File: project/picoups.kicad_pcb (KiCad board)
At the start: 4 copper layers, 65 x 30 mm, 73 parts, among them J1 VIN, J2 BATT, J3 USB_C_Receptacle, J4 Conn_02x20_Odd_Even, Q1 Q_PMOS_GSD, SW1 SW_5V, SW2 SW_USER, U1 LT3652EMSE, U2 TPS2116, U3 TPS61235P, U4 BQ24040, U5 INA3221, U6 M41T62

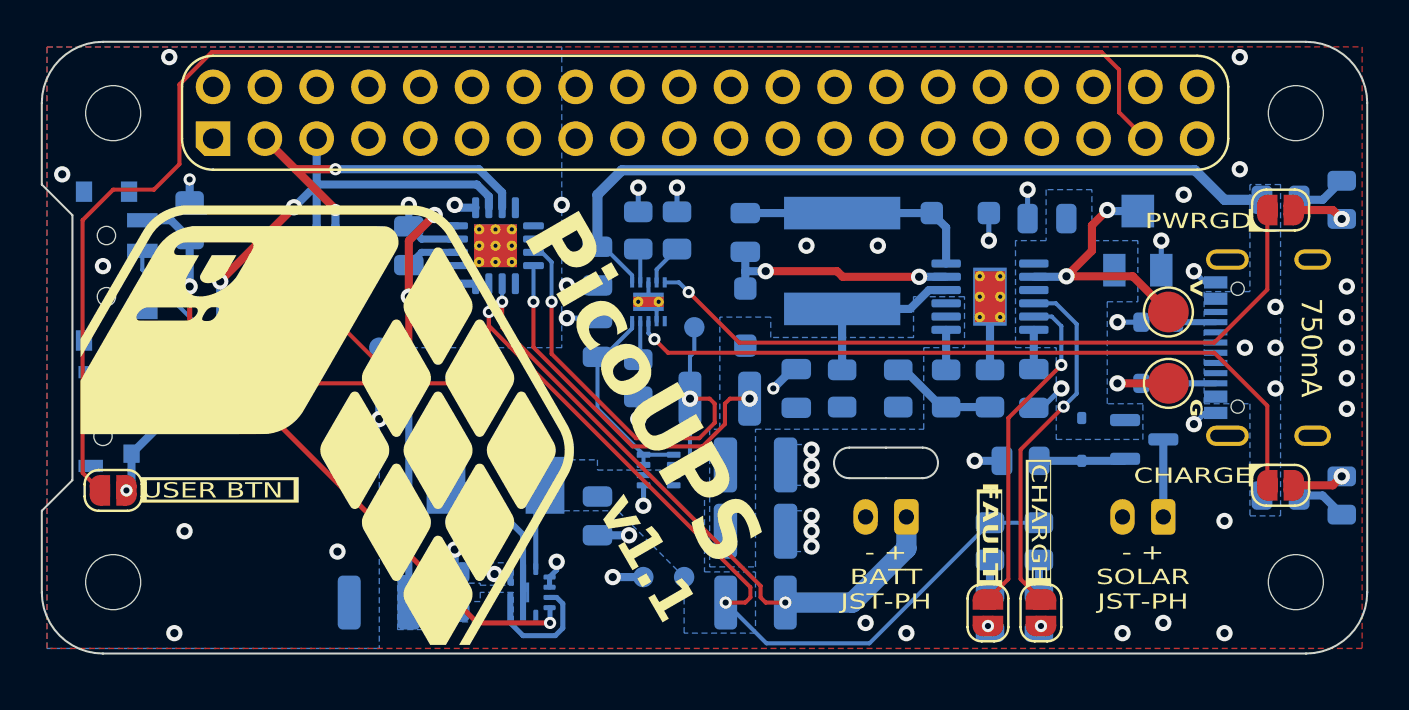
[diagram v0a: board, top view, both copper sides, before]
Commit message: Fixed solar status LEDs wrong VBAT
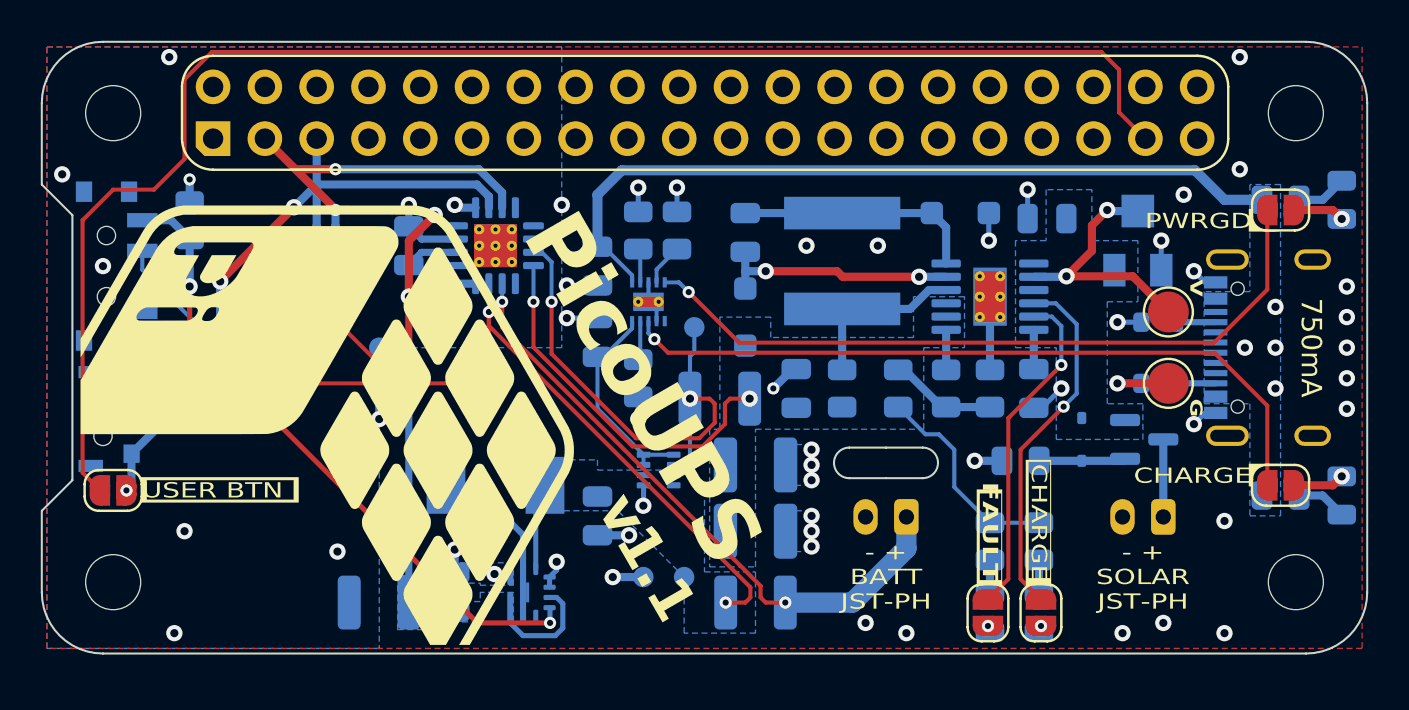
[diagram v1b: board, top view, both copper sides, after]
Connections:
- J4 pad 1: 3v3 -> unconnected-(J4-Pin_1-Pad1)
- R16 pad 2: VBAT+ -> VBAT_SOL+
- R17 pad 2: VBAT+ -> VBAT_SOL+
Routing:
- net VBAT+: track 74.3 -> 55.6 mm
- net VBAT_SOL+: track 18.2 -> 28.5 mm
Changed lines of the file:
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@@
   (net 29 "unconnected-(J3-SBU2-PadB8)")
   (net 30 "unconnected-(J3-SHIELD-PadS1)")
-  (net 31 "3v3")
+  (net 31 "unconnected-(J4-Pin_1-Pad1)")
   (net 32 "5V")
   (net 33 "SDA")
@@
     (pad "1" thru_hole roundrect (at -2.54 0 90) (size 1.7 1.7) (drill 1) (layers "*.Cu" "*.Mask") (roundrect_rratio 0)
       (chamfer_ratio 0.25) (chamfer top_left)
-      (net 31 "3v3") (pinfunction "Pin_1") (pintype "passive"))
+      (net 31 "unconnected-(J4-Pin_1-Pad1)") (pinfunction "Pin_1") (pintype "passive+no_connect"))
     (pad "2" thru_hole circle (at 0 0 90) (size 1.7 1.7) (drill 1) (layers "*.Cu" "*.Mask")
       (net 32 "5V") (pinfunction "Pin_2") (pintype "passive"))
@@
     (pad "17" thru_hole circle (at 0.8 0.8) (size 0.5 0.5) (drill 0.2) (layers "*.Cu")
       (net 1 "GND") (pinfunction "EP") (pintype "passive"))
-    (model "${KICAD7_3DMODEL_DIR}/Package_DFN_QFN.3dshapes/QFN-16-1EP_4x4mm_P0.65mm_EP2.1x2.1mm.step"
+    (model "${KICAD6_3DMODEL_DIR}/Package_DFN_QFN.3dshapes/Texas_RGV_S-PVQFN-N16_EP2.1x2.1mm.wrl"
       (offset (xyz 0 0 0))
       (scale (xyz 1 1 1))
@@
       (net 15 "Net-(D5-A)") (pintype "passive"))
     (pad "2" smd roundrect (at 0.9125 0 90) (size 1.025 1.4) (layers "B.Cu" "B.Paste" "B.Mask") (roundrect_rratio 0.243902439)
-      (net 7 "VBAT+") (pintype "passive"))
+      (net 3 "VBAT_SOL+") (pintype "passive"))
     (model "${KICAD6_3DMODEL_DIR}/Resistor_SMD.3dshapes/R_0805_2012Metric.wrl"
       (offset (xyz 0 0 0))
@@
       (net 13 "Net-(D4-A)") (pintype "passive"))
     (pad "2" smd roundrect (at 0.9125 0 90) (size 1.025 1.4) (layers "B.Cu" "B.Paste" "B.Mask") (roundrect_rratio 0.243902439)
-      (net 7 "VBAT+") (pintype "passive"))
+      (net 3 "VBAT_SOL+") (pintype "passive"))
     (model "${KICAD6_3DMODEL_DIR}/Resistor_SMD.3dshapes/R_0805_2012Metric.wrl"
       (offset (xyz 0 0 0))
@@
   (via (at 115.1125 104.75) (size 0.6) (drill 0.3) (layers "F.Cu" "B.Cu") (net 3))
   (via (at 125.7125 109.5) (size 0.8) (drill 0.4) (layers "F.Cu" "B.Cu") (net 3))
+  (segment (start 137.5 115.5875) (end 135.75 113.8375) (width 0.2) (layer "B.Cu") (net 3))
+  (segment (start 134.3375 111.25) (end 133 109.9125) (width 0.2) (layer "B.Cu") (net 3))
+  (segment (start 135.75 113.8375) (end 135.75 112) (width 0.2) (layer "B.Cu") (net 3))
+  (segment (start 139.9 115.5875) (end 137.5 115.5875) (width 0.2) (layer "B.Cu") (net 3))
+  (segment (start 135.75 112) (end 135 111.25) (width 0.2) (layer "B.Cu") (net 3))
   (segment (start 115.1125 104.75) (end 115.1125 102.975) (width 0.2) (layer "B.Cu") (net 3))
+  (segment (start 135 111.25) (end 134.3375 111.25) (width 0.2) (layer "B.Cu") (net 3))
   (segment (start 134.644916 100.4) (end 130.25 100.4) (width 0.4) (layer "B.Cu") (net 4))
   (segment (start 135.35 102.875) (end 135.35 101.105084) (width 0.4) (layer "B.Cu") (net 4))
@@
   (via (at 124.5375 119.5) (size 0.6) (drill 0.3) (layers "F.Cu" "B.Cu") (net 7))
   (via (at 99 106.25) (size 0.6) (drill 0.3) (layers "F.Cu" "B.Cu") (net 7))
-  (segment (start 131.5875 121.5) (end 126.5375 121.5) (width 0.2) (layer "B.Cu") (net 7))
   (segment (start 112.925 105.25) (end 112.925 103.8625) (width 0.2) (layer "B.Cu") (net 7))
   (segment (start 115.225 117.85) (end 115.225 114.2015) (width 0.25) (layer "B.Cu") (net 7))
-  (segment (start 137.5 115.5875) (end 131.5875 121.5) (width 0.2) (layer "B.Cu") (net 7))
   (segment (start 104.48 104.73) (end 104.48 103.85) (width 0.2) (layer "B.Cu") (net 7))
   (segment (start 115.225 114.2015) (end 115.6765 113.75) (width 0.25) (layer "B.Cu") (net 7))
-  (segment (start 139.9 115.5875) (end 137.5 115.5875) (width 0.2) (layer "B.Cu") (net 7))
   (segment (start 95.93 103.18) (end 95.93 102.25) (width 0.2) (layer "B.Cu") (net 7))
-  (segment (start 126.5375 121.5) (end 124.5375 119.5) (width 0.2) (layer "B.Cu") (net 7))
   (segment (start 99 106.25) (end 95.93 103.18) (width 0.2) (layer "B.Cu") (net 7))
   (segment (start 109 104.5) (end 109 107.75) (width 0.35) (layer "F.Cu") (net 8))
@@
   (segment (start 95.15 114) (end 95.4 113.75) (width 0.4) (layer "B.Cu") (net 34))
   (segment (start 99.75 103.75) (end 99.75 107.85) (width 0.4) (layer "B.Cu") (net 34))
-  (segment (start 143.83 93.366117) (end 143.83 95.46) (width 0.2) (layer "F.Cu") (net 59))
-  (segment (start 93.85 113.984314) (end 93 113.134314) (width 0.2) (layer "F.Cu") (net 59))
-  (segment (start 97.75 94.092233) (end 99.342233 92.5) (width 0.2) (layer "F.Cu") (net 59))
-  (segment (start 97.75 98) (end 97.75 94.092233) (width 0.2) (layer "F.Cu") (net 59))
   (segment (start 93 113.134314) (end 93 100.75) (width 0.2) (layer "F.Cu") (net 59))
-  (segment (start 99.342233 92.5) (end 142.963883 92.5) (width 0.2) (layer "F.Cu") (net 59))
-  (segment (start 94.5 99.25) (end 96.5 99.25) (width 0.2) (layer "F.Cu") (net 59))
-  (segment (start 96.5 99.25) (end 97.75 98) (width 0.2) (layer "F.Cu") (net 59))
-  (segment (start 143.83 95.46) (end 145.12 96.75) (width 0.2) (layer "F.Cu") (net 59))
   (segment (start 93 100.75) (end 94.5 99.25) (width 0.2) (layer "F.Cu") (net 59))
   (segment (start 142.963883 92.5) (end 143.83 93.366117) (width 0.2) (layer "F.Cu") (net 59))
+  (segment (start 98 93.842233) (end 99.342233 92.5) (width 0.2) (layer "F.Cu") (net 59))
+  (segment (start 98 97.75) (end 98 93.842233) (width 0.2) (layer "F.Cu") (net 59))
+  (segment (start 143.83 93.366117) (end 143.83 95.46) (width 0.2) (layer "F.Cu") (net 59))
+  (segment (start 94.5 99.25) (end 96.5 99.25) (width 0.2) (layer "F.Cu") (net 59))
+  (segment (start 143.83 95.46) (end 145.12 96.75) (width 0.2) (layer "F.Cu") (net 59))
+  (segment (start 96.5 99.25) (end 98 97.75) (width 0.2) (layer "F.Cu") (net 59))
+  (segment (start 99.342233 92.5) (end 142.963883 92.5) (width 0.2) (layer "F.Cu") (net 59))
+  (segment (start 93.85 113.984314) (end 93 113.134314) (width 0.2) (layer "F.Cu") (net 59))
   (segment (start 141 107.8495) (end 138.4 110.4495) (width 0.2) (layer "F.Cu") (net 62))
   (segment (start 138.4 118.35) (end 137.4 119.35) (width 0.2) (layer "F.Cu") (net 62))

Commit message: Moved 5V supply
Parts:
- added TP7: GND, TestPoint:TestPoint_Pad_D1.0mm, B.Cu at (116.2, 109.8)
- added TP9: 5V, TestPoint:TestPoint_Pad_D1.0mm, B.Cu at (116.2, 107.8)
- moved TP6 13.4 mm to (114.2, 107.8)
- moved TP5 10.6 mm to (114.2, 109.8)
- moved C7 5.76 mm to (121.5, 120.0), turned to 180 degrees
- moved TP3 4.71 mm to (112.2, 107.8)
- moved TP4 4.71 mm to (112.2, 109.8)
- moved C8 2.50 mm to (113.8, 119.0)
- moved L2 2.50 mm to (115.8, 113.8)
- moved U3 2.50 mm to (117.2, 119.0)
- moved R11 2.46 mm to (110.0, 119.5)
- moved U6 0.75 mm to (104.9, 101.8)
- moved R8 0.25 mm to (120.5, 108.5)
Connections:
- net /Power Mux/USB renamed VBAT_USB
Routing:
- net Net-(SW1-C): track 31.7 -> 40.0 mm
- net VBAT+: track 55.6 -> 50.3 mm
- net VBAT_USB: track 10.3 -> 12.5 mm
- net GND: track 45.6 -> 44.5 mm, vias 61 -> 35
- net SDA: track 17.3 -> 16.2 mm
- net 5V+: track 30.8 -> 31.9 mm, vias 3 -> 4
- net SCL: track 32.5 -> 31.8 mm
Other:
- board text added: "5"
- board text added: "B"
- board text added: "U"
- board text removed: "5V"
- board text removed: "GND"
- board text removed: "VBAT"

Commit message: Dimmed the USB status LEDs (again)
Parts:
- R18, R19: value 500 -> 1k
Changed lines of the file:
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@@
         (effects (font (size 0.6 0.8) (thickness 0.15)) (justify mirror))
     )
-    (fp_text value "500" (at 0 -1.65) (layer "B.Fab")
+    (fp_text value "1k" (at 0 -1.65) (layer "B.Fab")
         (effects (font (size 1 1) (thickness 0.15)) (justify mirror))
     )
@@
         (effects (font (size 0.6 0.8) (thickness 0.15) bold) (justify mirror))
     )
-    (fp_text value "500" (at 0 -1.65) (layer "B.Fab")
-        (effects (font (size 1 1) (thickness 0.15)) (justify mirror))
-    )
+    (fp_text value "1k" (at 0 -1.65) (layer "B.Fab")
+        (effects (font (size 1 1) (thickness 0.15)) (justify mirror))
+    )

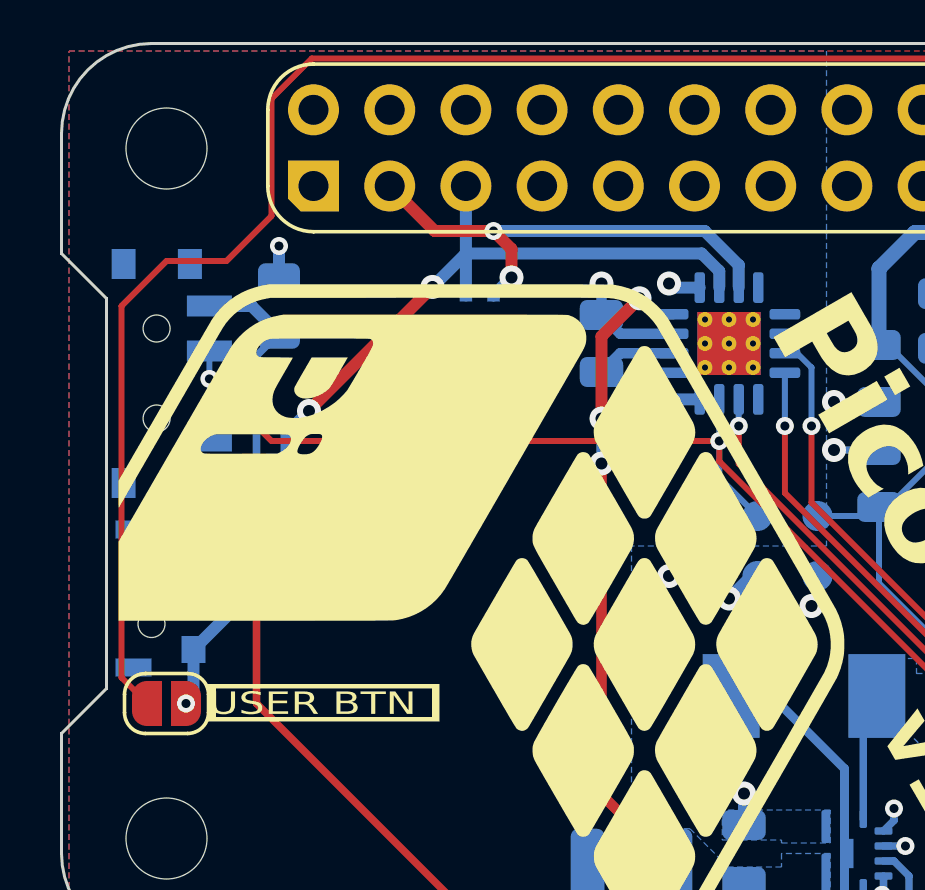
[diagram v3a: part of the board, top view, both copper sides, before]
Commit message: Added RTC wake
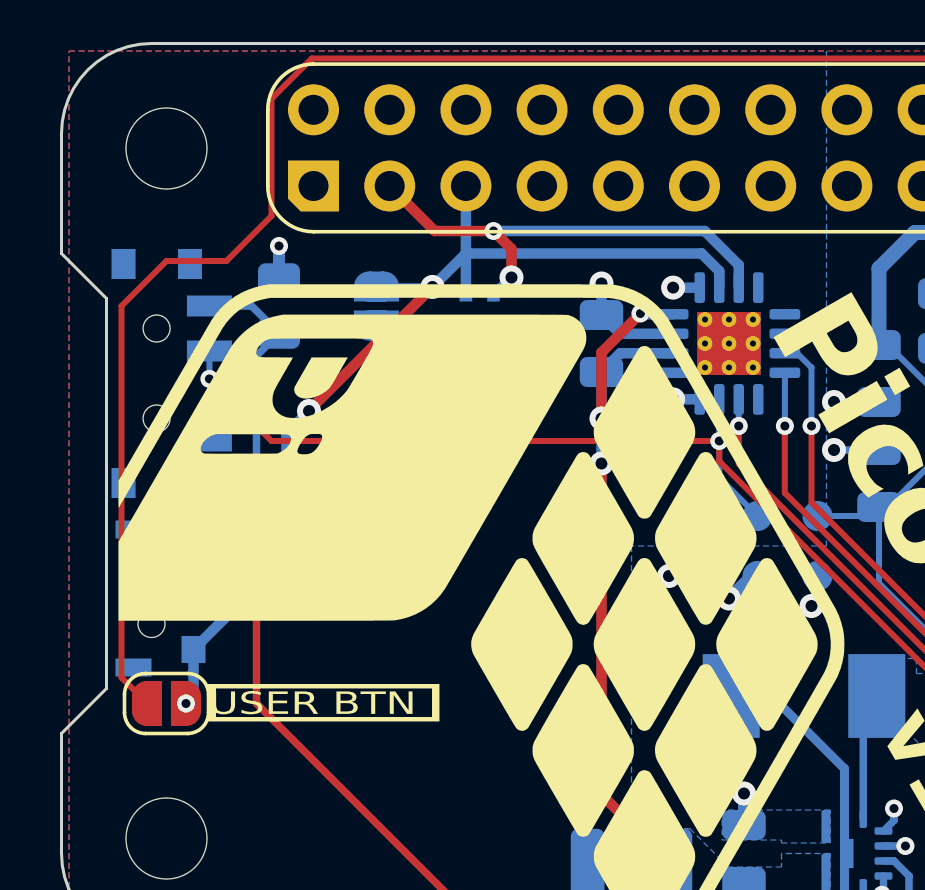
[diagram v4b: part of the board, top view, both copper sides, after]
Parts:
- added JP6: USER, Jumper:SolderJumper-2_P1.3mm_Open_RoundedPad1.0x1.5mm, B.Cu at (101.5, 100.8)
- moved G*** 1.00 mm to (100.8, 109.2)
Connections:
- U6 pad 6: unconnected-(U6-~{IRQ}/OUT-Pad6) -> WAKEUP
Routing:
- net WAKEUP: track 0.00 -> 3.31 mm
- net SCL: track 31.8 -> 33.6 mm
- net 5V+: track 31.9 -> 31.1 mm
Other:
- board text added: "RTC WAKE"

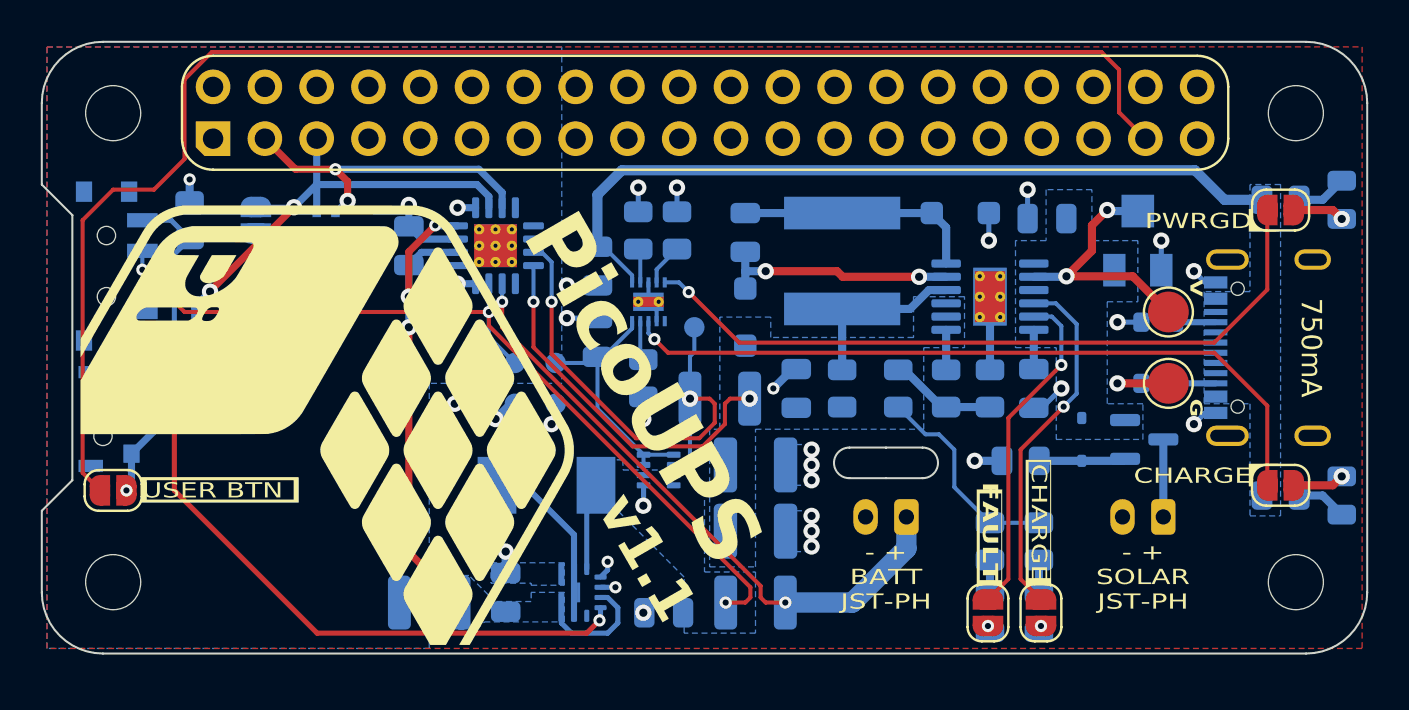
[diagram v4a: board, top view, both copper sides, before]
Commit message: Added output capacitors
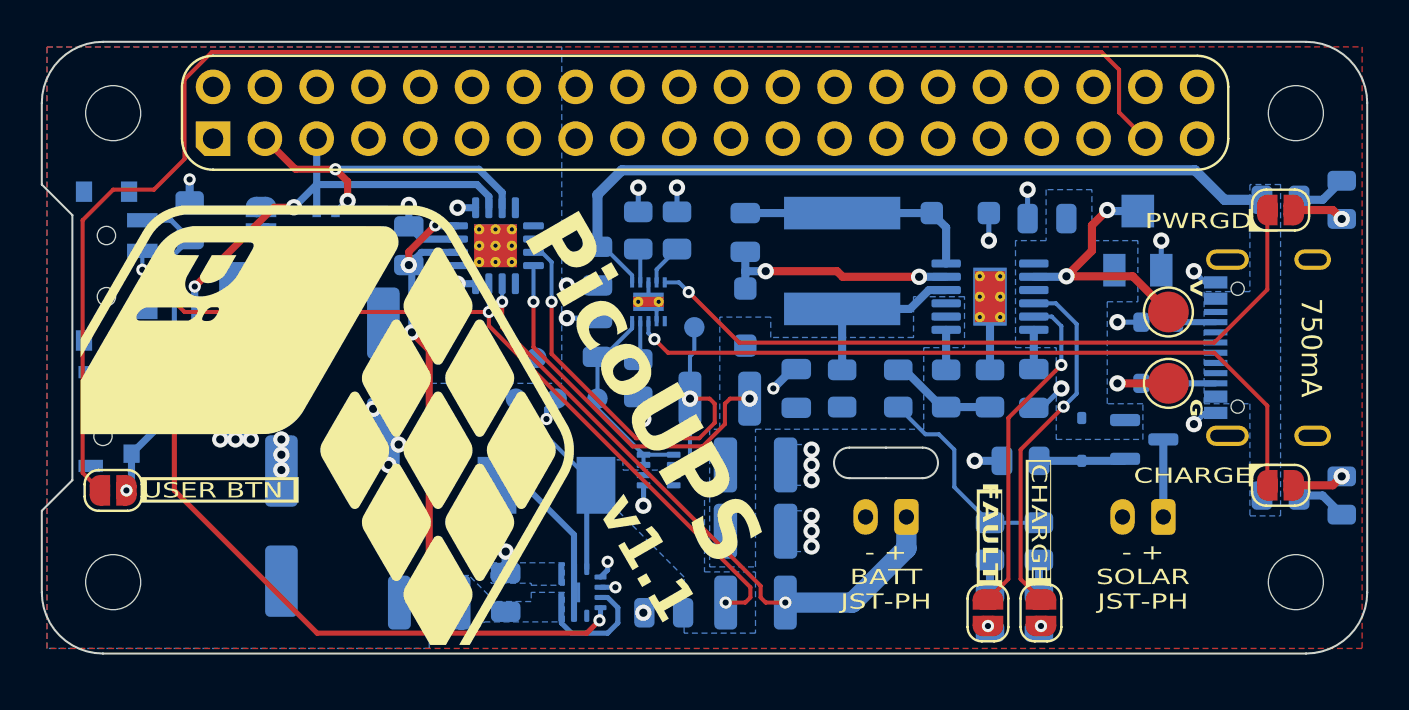
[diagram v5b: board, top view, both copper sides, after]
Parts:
- removed the G*** at (105.2, 111.2)
- removed the G*** at (100.8, 109.2)
- removed the REF** at (101.2, 118.0)
- removed TP4, TP7: GND, TestPoint:TestPoint_Pad_D1.0mm
- added C12: 270uF, Capacitor_SMD:CP_Elec_6.3x5.8, B.Cu at (102.8, 115.8)
- added C13: 470uF, Capacitor_SMD:CP_Elec_6.3x7.7, B.Cu at (107.8, 108.5)
- added C14: 470uF, Capacitor_SMD:CP_Elec_6.3x7.7, B.Cu at (100.5, 107.2)
- moved TP3 3.06 mm to (115.2, 107.5)
- moved TP9 2.70 mm to (118.2, 109.5)
- moved TP5 2.07 mm to (116.2, 109.5), turned to 180 degrees
- moved TP6 1.75 mm to (114.2, 109.5)
- moved JP6 0.25 mm to (101.8, 100.8)
- moved R8 0.25 mm to (120.2, 108.5)
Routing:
- net VBAT+: track 50.3 -> 53.1 mm
- net VBAT_USB: track 12.5 -> 10.3 mm
- net GND: track 44.1 -> 42.0 mm, vias 35 -> 42
- net 5V+: track 31.1 -> 29.6 mm
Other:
- board text added: "WAKE"
- board text added: "rev 1.1.1 16.09.23"
- board text added: "Διονύσης Τουλάτος"
- board text removed: "RTC WAKE"
- board text removed: "rev 1.1.1 16.09.23 Διονύσης Τουλάτος"
